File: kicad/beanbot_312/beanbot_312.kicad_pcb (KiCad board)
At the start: 2 copper layers, 100 x 84 mm, 51 parts, among them M1 P&O2_MEETPUNT, M10 P&O2_RGB_LED, M11 P&O2_RESISTOR, M12 P&O2_MEETPUNT, M13 P&O2_RESISTOR, M14 P&O2_MOSFET, M15 P&O2_RESISTOR, M16 P&O2_ULTRASONE_HC_SR04, M17 P&O2_MEETPUNT, M18 P&O2_MEETPUNT, M19 P&O2_MEETPUNT, M2 P&O2_MEETPUNT, M20 P&O2_MEETPUNT, M21 P&O2_GEWICHTSENSOR2, M23 P&O2_MEETPUNT, M24 P&O2_MEETPUNT, M25 P&O2_KLEURSENSOR, M26 P&O2_MEETPUNT, M27 P&O2_MEETPUNT, M28 P&O2_MEETPUNT, M29 P&O2_RELAIS-DP, M3 P&O2_RESISTOR, M30 P&O2_DC-MOTOR, M31 P&O2_RELAIS-DP, M32 P&O2_DC-MOTOR, M33 P&O2_RELAIS-DP, M34 P&O2_DC-MOTOR, M35 P&O2_DIODE, M36 P&O2_DIODE, M37 P&O2_DIODE, M38 P&O2_MEETPUNT, M39 P&O2_MEETPUNT, M4 P&O2_MOSFET, M40 P&O2_MEETPUNT, M41 P&O2_MEETPUNT, M42 P&O2_MEETPUNT, M43 P&O2_MEETPUNT, M44 P&O2_RESISTOR, M45 P&O2_RESISTOR, M46 P&O2_RESISTOR, M47 P&O2_MOSFET, M48 P&O2_MOSFET, M49 P&O2_MOSFET, M5 P&O2_RESISTOR, M50 P&O2_MEETPUNT, M51 P&O2_MEETPUNT, M52 P&O2_MEETPUNT, M6 P&O2_MEETPUNT, M7 P&O2_RESISTOR, M8 P&O2_MOSFET, M9 P&O2_RESISTOR

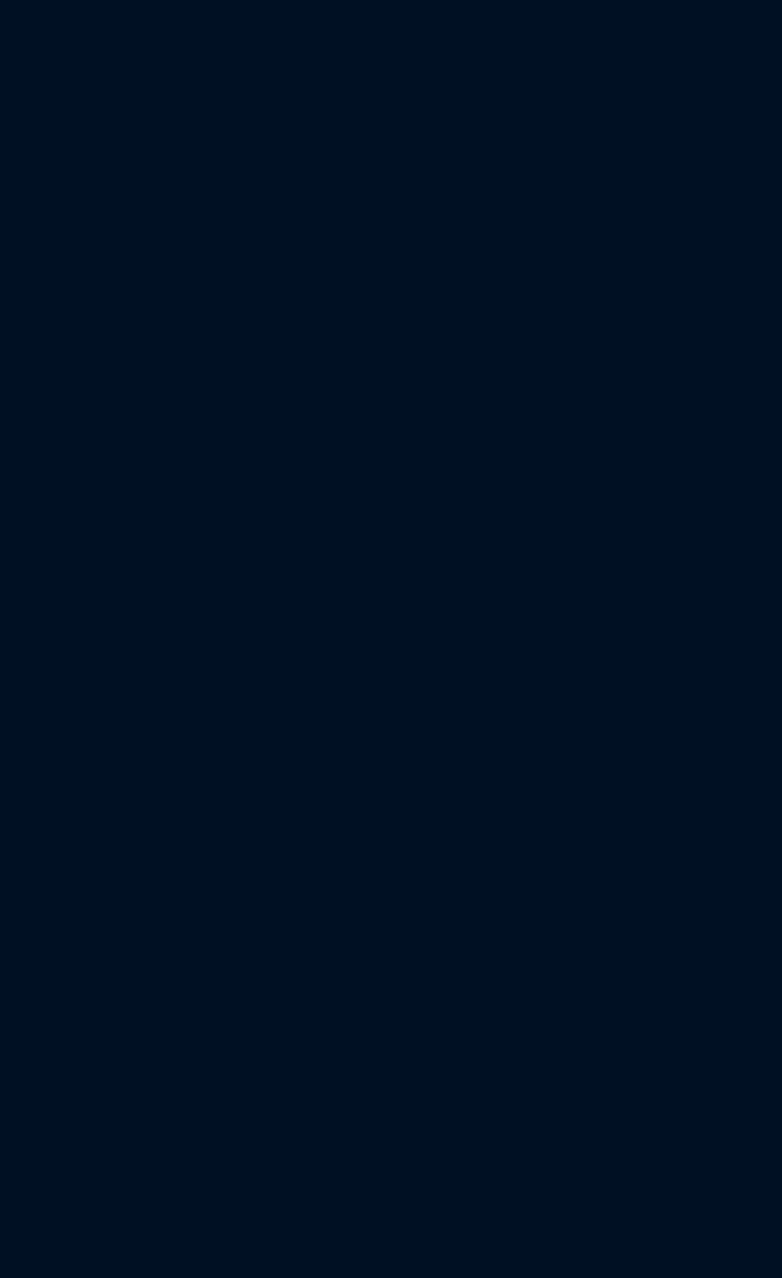
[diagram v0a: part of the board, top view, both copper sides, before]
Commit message: Added footprints
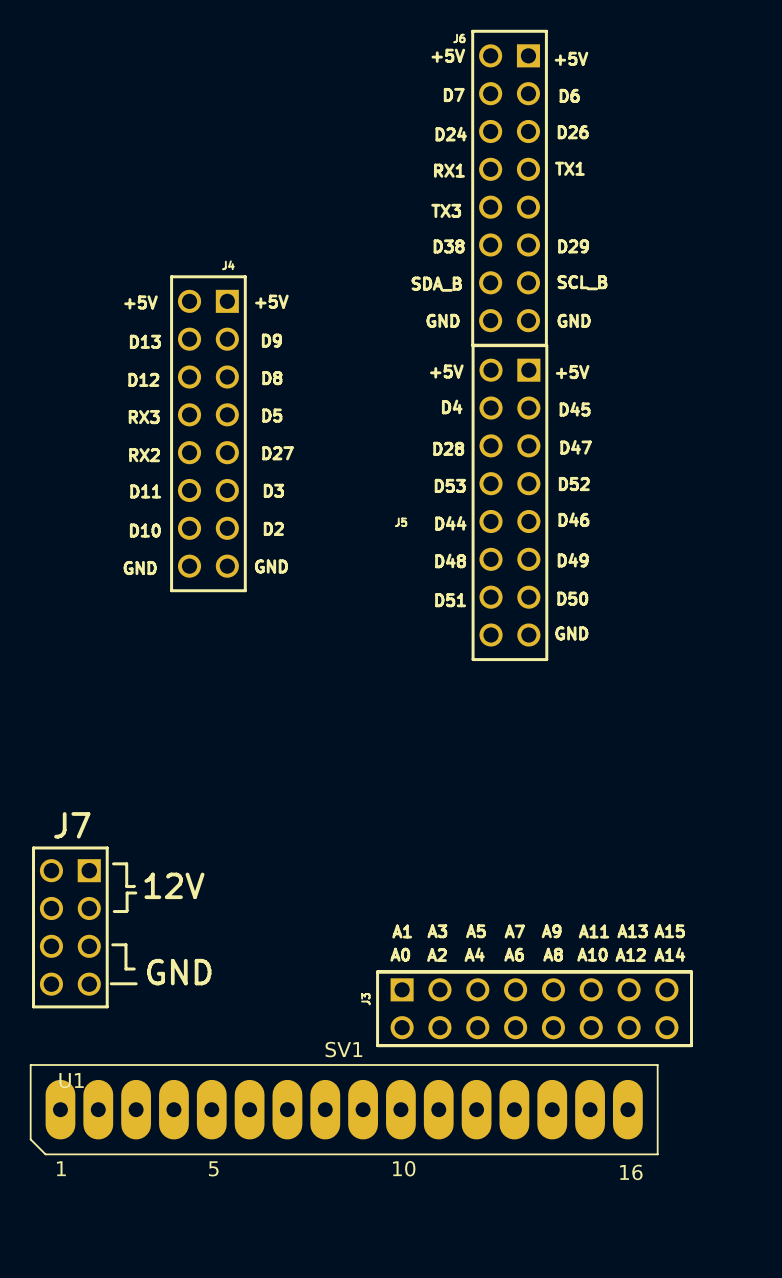
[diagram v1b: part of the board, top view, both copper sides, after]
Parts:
- added SV1: P&O2_LCD, 1_P&O2_lib:P&O2_LCD, F.Cu at (65.0, 110.0)
- added U1: P&O2_ARDUINO_MEGA_SHIELD, 1_P&O2_lib:P&O2_ARDUINO_MEGA_SHIELD, F.Cu at (44.1, 103.1)

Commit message: Updated pcb
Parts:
- removed M33: P&O2_RELAIS-DP, 1_P&O2_lib:P&O2_RELAY-DP
- removed M34: P&O2_DC-MOTOR, 1_P&O2_lib:P&O2_2PIN-SCREW-5.08
- removed M37: P&O2_DIODE, 1_P&O2_lib:P&O2_DIODE
- removed M40, M43, M52: P&O2_MEETPUNT, 1_P&O2_lib:P&O2_MEETPUNT
- removed M46: P&O2_RESISTOR, 1_P&O2_lib:P&O2_RESISTOR
- removed M49: P&O2_MOSFET, 1_P&O2_lib:P&O2_TO220
- moved SV1 118.3 mm to (183.0, 118.9), turned to 90 degrees
- moved U1 95.8 mm to (131.9, 141.5)
- moved M11 58.0 mm to (194.0, 113.0), turned to -90 degrees
- moved M19 41.1 mm to (156.0, 126.5)
- moved M20 41.1 mm to (156.0, 121.2)
- moved M21 41.1 mm to (150.0, 128.0)
- moved M18 36.3 mm to (115.8, 133.0)
- moved M16 36.3 mm to (110.3, 127.0)
- moved M17 36.3 mm to (108.5, 133.0)
- moved M28 31.7 mm to (120.8, 141.0)
- moved M27 30.9 mm to (113.3, 141.0)
- moved M1 30.0 mm to (106.0, 141.0)
- moved M25 3.08 mm to (132.4, 87.8)
- moved M23 3.08 mm to (143.0, 77.0)
- moved M24 3.08 mm to (143.0, 81.3)
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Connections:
- U1 pad 21: /PWM_LEDR -> unconnected-(U1-Pad21)
- U1 pad 22: unconnected-(U1-Pad22) -> /PWM_LEDB
- U1 pad 24: unconnected-(U1-Pad24) -> /PWM_LEDG
- U1 pad 27: /D_RELM3 -> unconnected-(U1-Pad27)
- U1 pad 28: /D_KS2 -> /D_UECHO
- U1 pad 29: /PWM_M2 -> unconnected-(U1-Pad29)
- U1 pad 30: /PWM_LEDB -> /PWM_LEDR
- U1 pad 31: /PWM_M1 -> unconnected-(U1-Pad31)
- U1 pad 32: /PWM_LEDG -> unconnected-(U1-Pad32)
- U1 pad 42: /PWM_M3 -> unconnected-(U1-Pad42)
- U1 pad 55: unconnected-(U1-Pad55) -> /PWM_M3
- U1 pad 56: unconnected-(U1-Pad56) -> /PWM_M2
- U1 pad 57: /D_RELM2 -> /D_RELM3
- U1 pad 58: /D_RELM1 -> /D_RELM2
- U1 pad 59: /D_KS3 -> unconnected-(U1-Pad59)
- U1 pad 60: /D_KOUT -> /D_KS3
- U1 pad 62: /D_UECHO -> /D_KS2
- U1 pad 64: unconnected-(U1-Pad64) -> /D_KOUT
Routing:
- net Net-(M33-Pad14): track 74.0 -> 0.00 mm
- net /12V: track 169.1 -> 116.2 mm
- net /PWM_LEDB: track 22.1 -> 65.7 mm
- net /PWM_M2: track 8.72 -> 39.0 mm
- net /PWM_M3: track 8.76 -> 38.0 mm
- net /PWM_LEDR: track 20.3 -> 48.5 mm
- net Net-(M33-Pad21): track 27.3 -> 0.00 mm
- net /PWM_LEDG: track 23.2 -> 49.9 mm
- net /D_RELM2: track 6.02 -> 31.8 mm
- net /D_KS3: track 7.27 -> 29.8 mm
- net /D_KS2: track 7.45 -> 29.2 mm
- net /D_KOUT: track 8.05 -> 29.2 mm
- net /5V: track 116.1 -> 136.9 mm
- net /D_RELM3: track 5.77 -> 26.1 mm
- net Net-(M33-Pad11): track 11.8 -> 0.00 mm
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- removed copper zone on B.Cu, net /GND
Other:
- board size 100 x 84 mm -> 100 x 101 mm

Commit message: Some progress on the PCB
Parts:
- moved M1 19.5 mm to (119.6, 127.0)
- moved M27 13.9 mm to (101.5, 133.8)
- moved M18 7.84 mm to (108.0, 134.2)
- moved M17 6.71 mm to (115.1, 134.4)
- moved M19 2.26 mm to (155.9, 124.2)
- moved M20 1.74 mm to (155.9, 119.5)
- turned M16 to 180 degrees
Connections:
- U1 pad 23: /PWM_UTRIG -> unconnected-(U1-Pad23)
- U1 pad 32: unconnected-(U1-Pad32) -> /PWM_UTRIG
- U1 pad 41: unconnected-(U1-Pad41) -> /D_LCDDB7
- U1 pad 43: unconnected-(U1-Pad43) -> /D_LCDDB6
- U1 pad 45: /D_LCDDB6 -> /D_LCDDB5
- U1 pad 46: /D_LCDDB7 -> unconnected-(U1-Pad46)
- U1 pad 47: unconnected-(U1-Pad47) -> /D_LCDDB4
- U1 pad 50: /D_LCDRS -> unconnected-(U1-Pad50)
- U1 pad 51: /D_LCDDB4 -> /D_LCDRS
- U1 pad 52: /D_LCDDB5 -> unconnected-(U1-Pad52)
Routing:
- net /12V: track 116.2 -> 210.3 mm
- net /D_WSCL: track 6.94 -> 57.1 mm
- net /D_UECHO: track 7.24 -> 54.2 mm
- net /PWM_UTRIG: track 6.72 -> 48.7 mm
- net /D_WSDA: track 6.22 -> 40.7 mm
- net /D_LCDRS: track 0.00 -> 32.2 mm
- net /D_LCDE: track 0.00 -> 29.5 mm
- net /5V: track 136.9 -> 162.8 mm
- net /D_LCDDB4: track 0.00 -> 19.4 mm
- net /D_LCDDB7: track 0.00 -> 19.4 mm
- net /D_LCDDB5: track 0.00 -> 19.4 mm
- net /D_LCDDB6: track 0.00 -> 19.4 mm

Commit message: Latest changes
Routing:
- added copper zone on B.Cu, net /GND
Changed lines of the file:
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@@
   (segment (start 175.22 104.92) (end 183 104.92) (width 1) (layer "F.Cu") (net 42))
   (segment (start 171.543612 101.243612) (end 175.22 104.92) (width 1) (layer "F.Cu") (net 42))
+  (zone (net 3) (net_name "/GND") (layer "B.Cu") (hatch edge 0.508)
+    (connect_pads (clearance 0.508))
+    (min_thickness 0.254) (filled_areas_thickness no)
+    (fill yes (thermal_gap 0.508) (thermal_bridge_width 0.508))
+    (polygon
+      (pts
+        (xy 198.85 144.9)
+        (xy 100.55 144.7)
+        (xy 101.4 46.3)
+        (xy 198.85 46.25)
+      )
+    )
+  )
 )

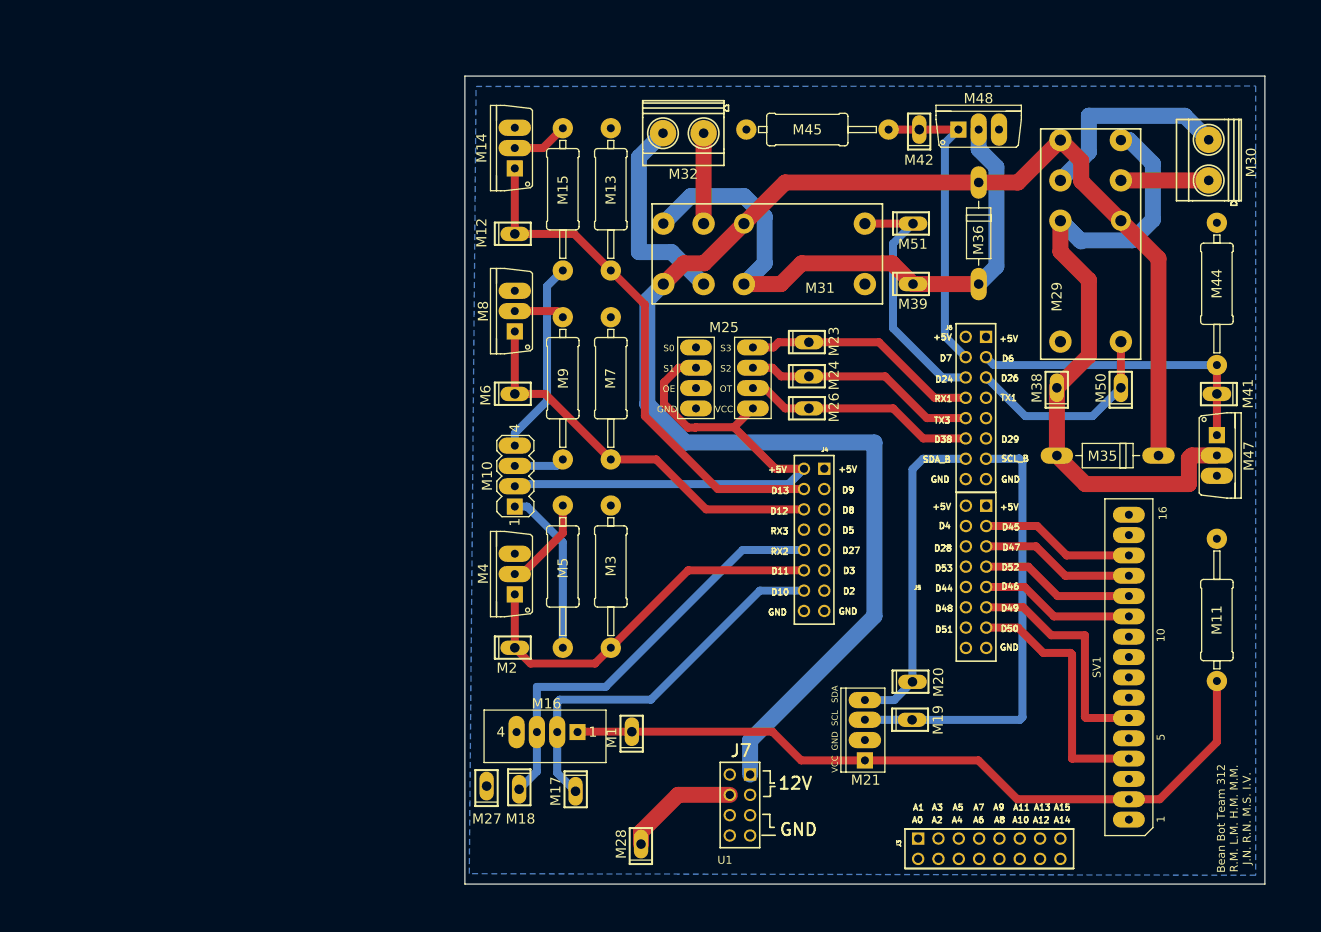
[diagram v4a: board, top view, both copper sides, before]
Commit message: Change border
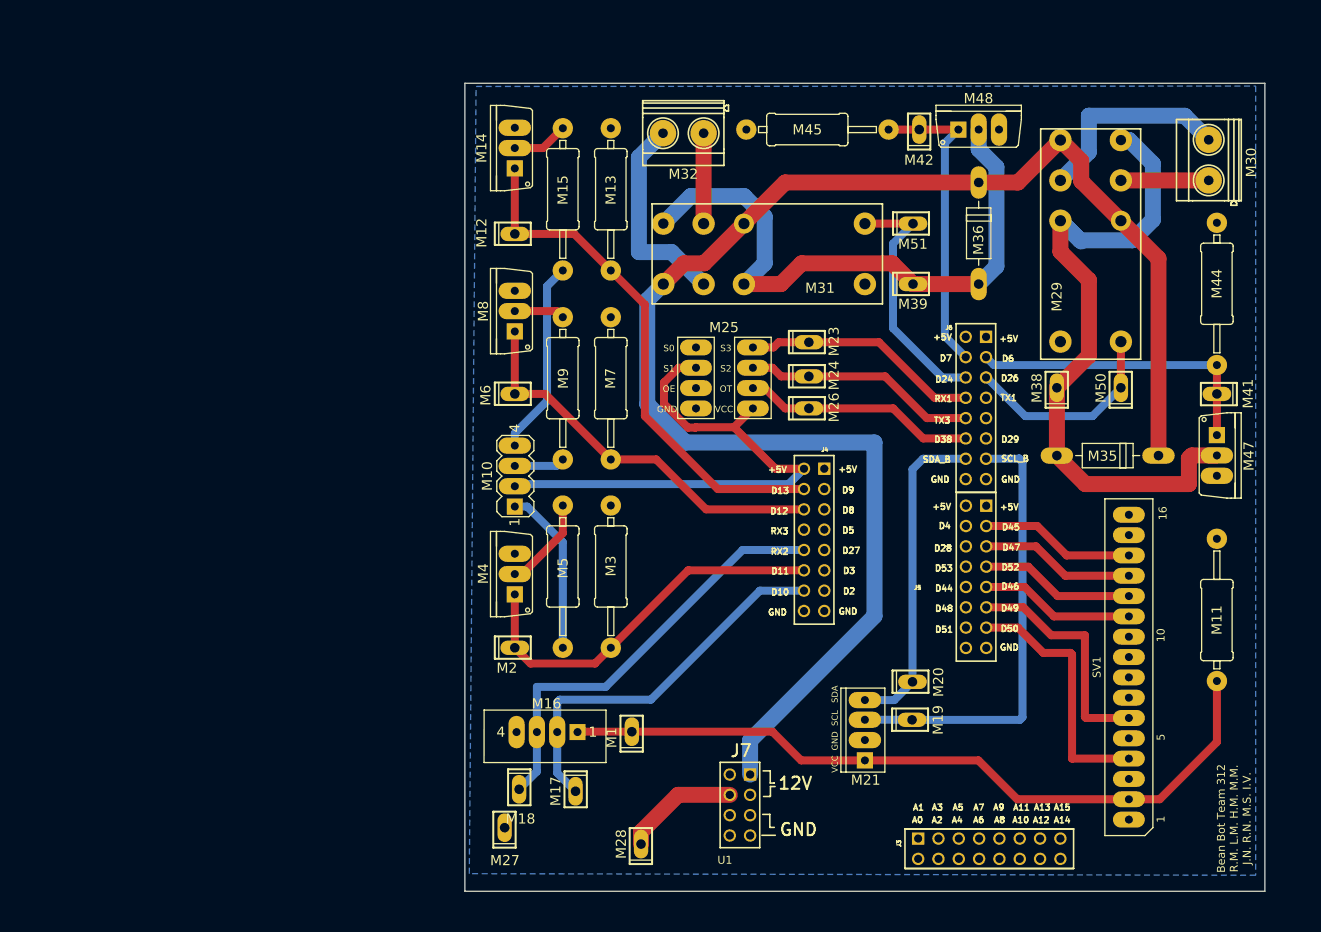
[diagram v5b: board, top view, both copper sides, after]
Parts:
- moved M27 5.67 mm to (103.7, 138.9)
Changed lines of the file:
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@@
   )
   (footprint "1_P&O2_lib:P&O2_MEETPUNT" (layer "F.Cu")
-    (at 101.45 133.75 180)
+    (at 103.7 138.95 180)
     (descr "PHOENIX CONNECTOR")
     (tags "PHOENIX CONNECTOR")
@@
       (net 19 "/D_KOUT") (pinfunction "TP") (pintype "input"))
   )
-  (gr_line (start 100 45) (end 100 146) (layer "Edge.Cuts") (width 0.1))
-  (gr_line (start 200 45) (end 100 45) (layer "Edge.Cuts") (width 0.1))
-  (gr_line (start 100 146) (end 200 146) (layer "Edge.Cuts") (width 0.1))
-  (gr_line (start 200 146) (end 200 45) (layer "Edge.Cuts") (width 0.1))
+  (gr_line (start 100 45.9) (end 100 146.9) (layer "Edge.Cuts") (width 0.1))
+  (gr_line (start 200 45.9) (end 100 45.9) (layer "Edge.Cuts") (width 0.1))
+  (gr_line (start 100 146.9) (end 200 146.9) (layer "Edge.Cuts") (width 0.1))
+  (gr_line (start 200 146.9) (end 200 45.9) (layer "Edge.Cuts") (width 0.1))
   (gr_text "Bean Bot Team 312\nR.M. L.M. H.M. M.M.\nJ.N. R.N. M.S. I.V." (at 196.15 137.8 90) (layer "F.SilkS")
     (effects (font (size 1 1) (thickness 0.15)))

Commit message: Finished PCB
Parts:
- M1, M12, M17, M18, M19, M2, M20, M23, M24, M26, M27, M28, M38, M39, M41, M42, M50, M51, M6: value P&O2_MEETPUNT -> >VALUE
- M10: value P&O2_RGB_LED -> >VALUE
- M11, M13, M15, M3, M44, M45, M5, M7, M9: value P&O2_RESISTOR -> >VALUE
- M35, M36: value P&O2_DIODE -> >VALUE
- moved M27 15.6 mm to (118.3, 133.3), turned to 0 degrees
- moved M28 8.10 mm to (122.0, 133.0)
- moved M17 2.57 mm to (112.8, 133.3)
- moved M11 1.36 mm to (194.0, 111.6)
- moved M1 0.90 mm to (119.6, 126.0)
- moved M10 0.90 mm to (106.2, 94.1)
- moved M16 0.90 mm to (110.3, 126.1)
- moved M19 0.90 mm to (155.9, 123.3)
- moved M20 0.90 mm to (155.9, 118.5)
- moved M21 0.90 mm to (150.0, 127.1)
- moved M23 0.90 mm to (143.0, 76.1)
- moved M25 0.90 mm to (132.4, 86.9)
- moved M31 0.90 mm to (137.4, 66.2)
- moved M36 0.90 mm to (164.2, 63.8)
- moved M38 0.90 mm to (172.7, 83.1)
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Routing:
- net /5V: track 162.8 -> 218.4 mm
- net Net-(M11-Pad1): track 0.00 -> 11.0 mm
- net /12V: track 210.3 -> 206.0 mm
- net /D_WSDA: track 40.7 -> 37.5 mm
- net /PWM_UTRIG: track 48.7 -> 47.6 mm
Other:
- board size 100 x 101 mm -> 100 x 100 mm
